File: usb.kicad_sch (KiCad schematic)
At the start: 16 parts, among them P1 USB_C_Plug_USB2.0, U1 MX6UL-VM, U4 TUSB320, U5 FPF2498BUCX, U6 TPD4EUSB30, U7 D5V0H1B2LP

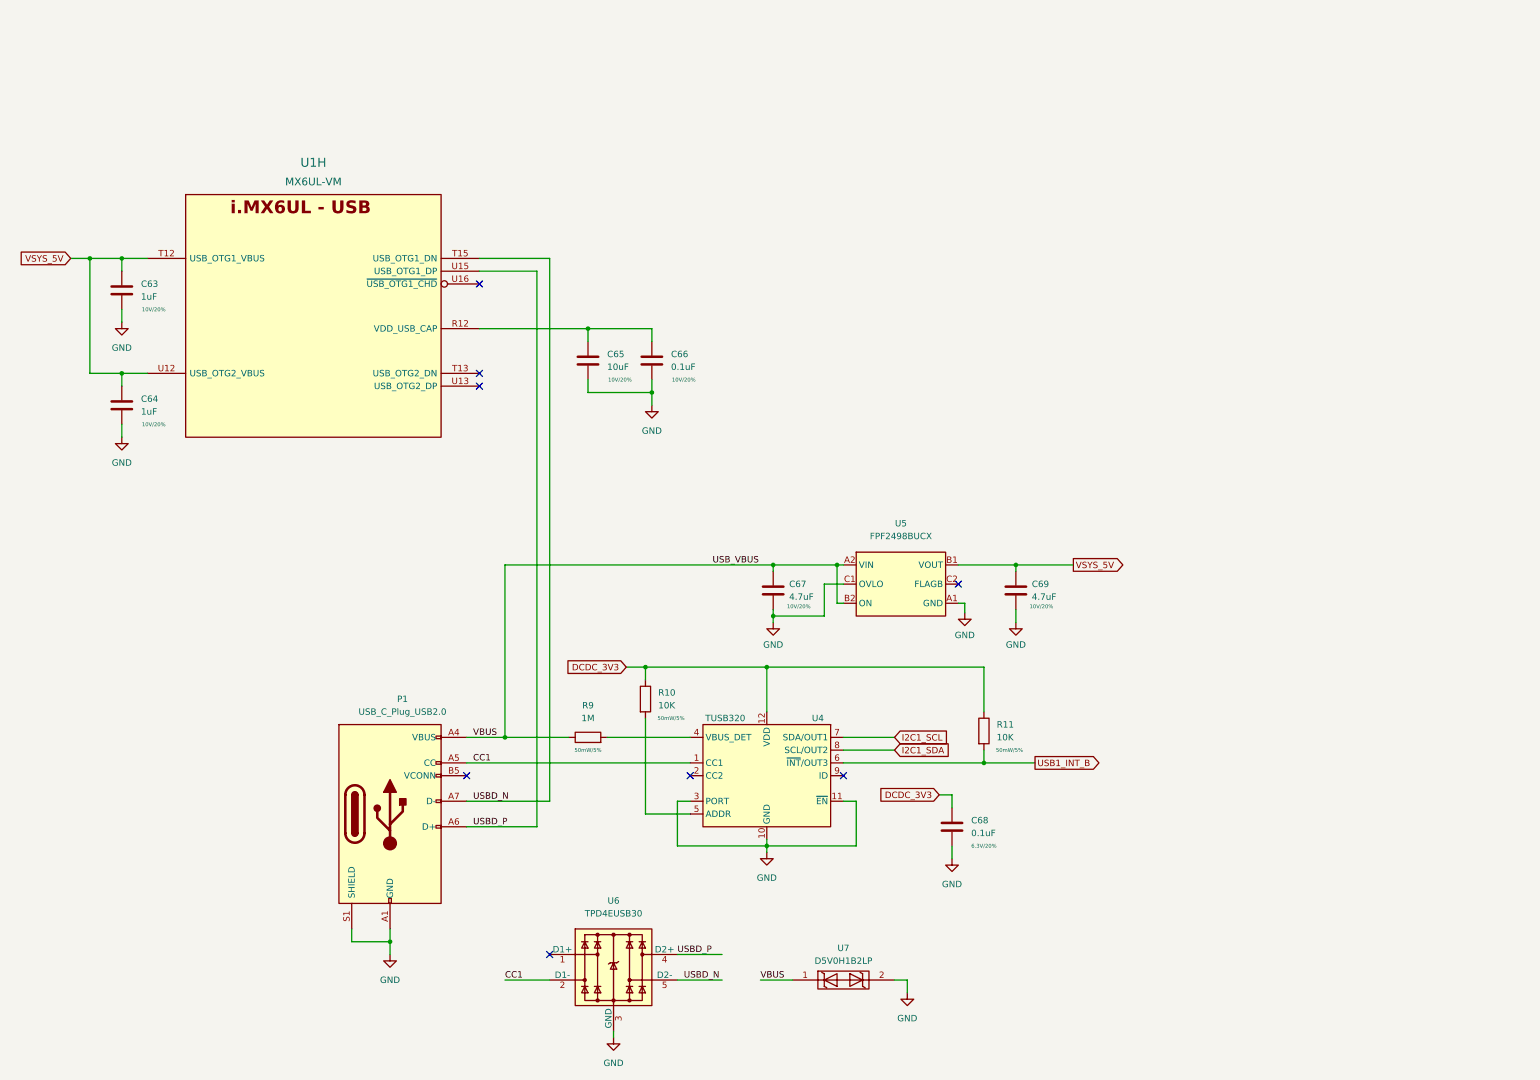
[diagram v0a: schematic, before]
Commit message: more ddr routing, add more connectors
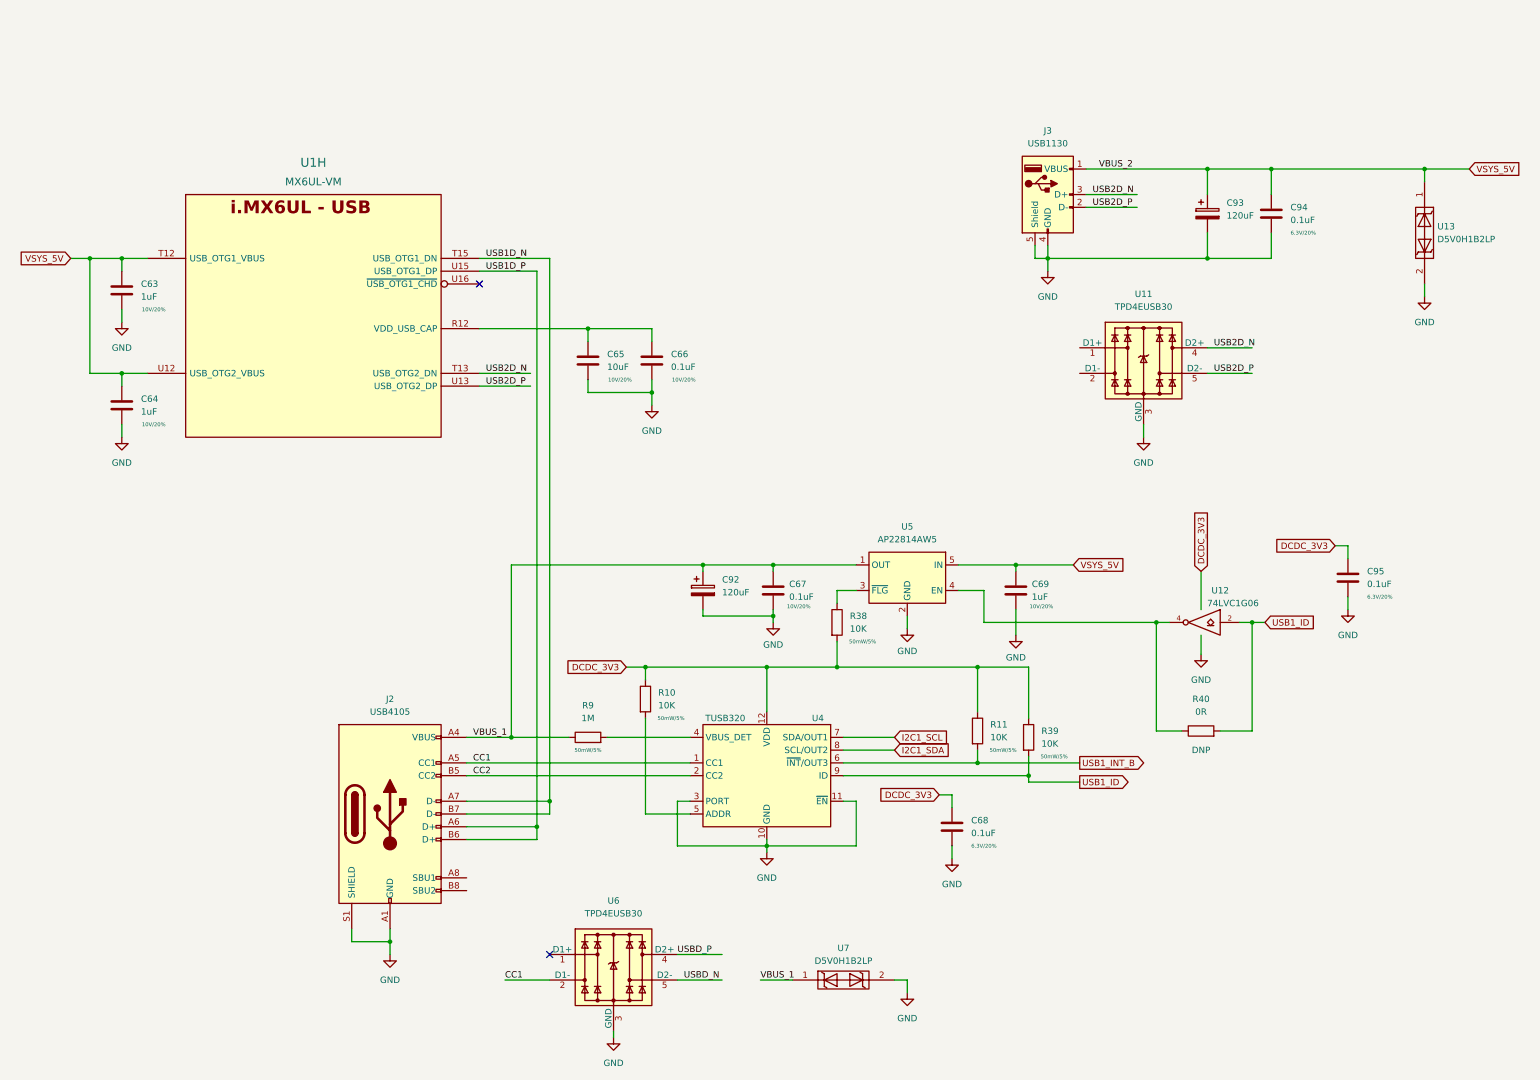
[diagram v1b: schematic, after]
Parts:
- removed P1: USB_C_Plug_USB2.0, Connector_USB:USB_C_Plug_Molex_105444, symbol Connector:USB_C_Plug_USB2.0
- removed U5: FPF2498BUCX, Package_CSP:WLCSP-6_1.4x1.0mm_P0.4mm, symbol imx6ull-sbc:FPF2498BUCX
- added C92, C93: 120uF, Capacitor_SMD:CP_Elec_5x5.8, symbol Device:C_Polarized
- added C94, C95: 0.1uF, Capacitor_SMD:C_0402_1005Metric, symbol Device:C
- added J2: USB4105, Connector_USB:USB_C_Receptacle_HRO_TYPE-C-31-M-12, symbol Connector:USB_C_Receptacle_USB2.0
- added J3: USB1130, imx6ull-sbc:GCT_USB1130-15-A_REVA, symbol Connector:USB_A
- added R38, R39: 10K, Resistor_SMD:R_0402_1005Metric, symbol Device:R
- added R40: 0R, Resistor_SMD:R_0402_1005Metric, symbol Device:R
- added U11: TPD4EUSB30, Package_SON:USON-10_2.5x1.0mm_P0.5mm, symbol imx6ull-sbc:TPD4EUSB30
- added U12: 74LVC1G06, Package_TO_SOT_SMD:SOT-23-5, symbol 74xGxx:74LVC1G06
- added U13: D5V0H1B2LP, imx6ull-sbc:DFN100X60X45-2N, symbol imx6ull-sbc:D5V0H1B2LP
- added U5: AP22814AW5, Package_TO_SOT_SMD:SOT-23-5, symbol Power_Management:AP22814AW5
- C66: footprint Capacitor_SMD:C_0402_1005Metric -> Capacitor_SMD:C_0201_0603Metric
- C67: value 4.7uF -> 0.1uF
- C69: value 4.7uF -> 1uF
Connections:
- net CC1: now also J2.A5 (CC1)
- net GND: now also C92.2, C93.2, C94.2, C95.2, J2.A1 (GND), J2.A12 (GND), J2.B1 (GND), J2.B12 (GND), J2.S1 (SHIELD), J3.4 (GND), J3.5 (Shield), U11.3 (GND), U11.8 (GND), U12.3 (GND), U13.2, U5.2 (GND)
- net USBD_N: no longer U1.T15 (USB_OTG1_DN)
- net USBD_P: no longer U1.U15 (USB_OTG1_DP)
- net VSYS_5V: now also C93.1, C94.1, J3.1 (VBUS), U13.1, U5.5 (IN)
- net USB2D_N: now reaches U1.T13 (USB_OTG2_DN)
- net USB2D_N: now also J3.3 (D+), U11.4 (D2+), U11.7
- net USB2D_P: now reaches U1.U13 (USB_OTG2_DP)
- net USB2D_P: now also J3.2 (D-), U11.5 (D2-), U11.6
- net CC2: now reaches U4.2 (CC2)
- net CC2: now also J2.B5 (CC2)
- net USB1_ID: now reaches U4.9 (ID)
- net USB1_ID: now also R39.2, R40.2, U12.2
- net DCDC_3V3 renamed VCC
- net VCC: now also C95.1, R38.2, R39.1, U12.5 (VCC)
- net USB_VBUS renamed VBUS_1
- net VBUS_1: now also C92.1, J2.A4 (VBUS), J2.A9 (VBUS), J2.B4 (VBUS), J2.B9 (VBUS), U5.1 (OUT)
- new net: R40.1, U12.4, U5.4 (EN)
- new net: R38.1, U5.3 (~{FLG})
- new net: U11.1 (D1+), U11.10
- new net: U11.2 (D1-), U11.9
- new net USB1D_N: J2.A7 (D-), J2.B7 (D-), U1.T15 (USB_OTG1_DN)
- new net USB1D_P: J2.A6 (D+), J2.B6 (D+), U1.U15 (USB_OTG1_DP)
- no-connect marks 8 -> 2
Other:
- moved on the sheet: R11

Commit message: start moving to hierarchal labels, add emmc
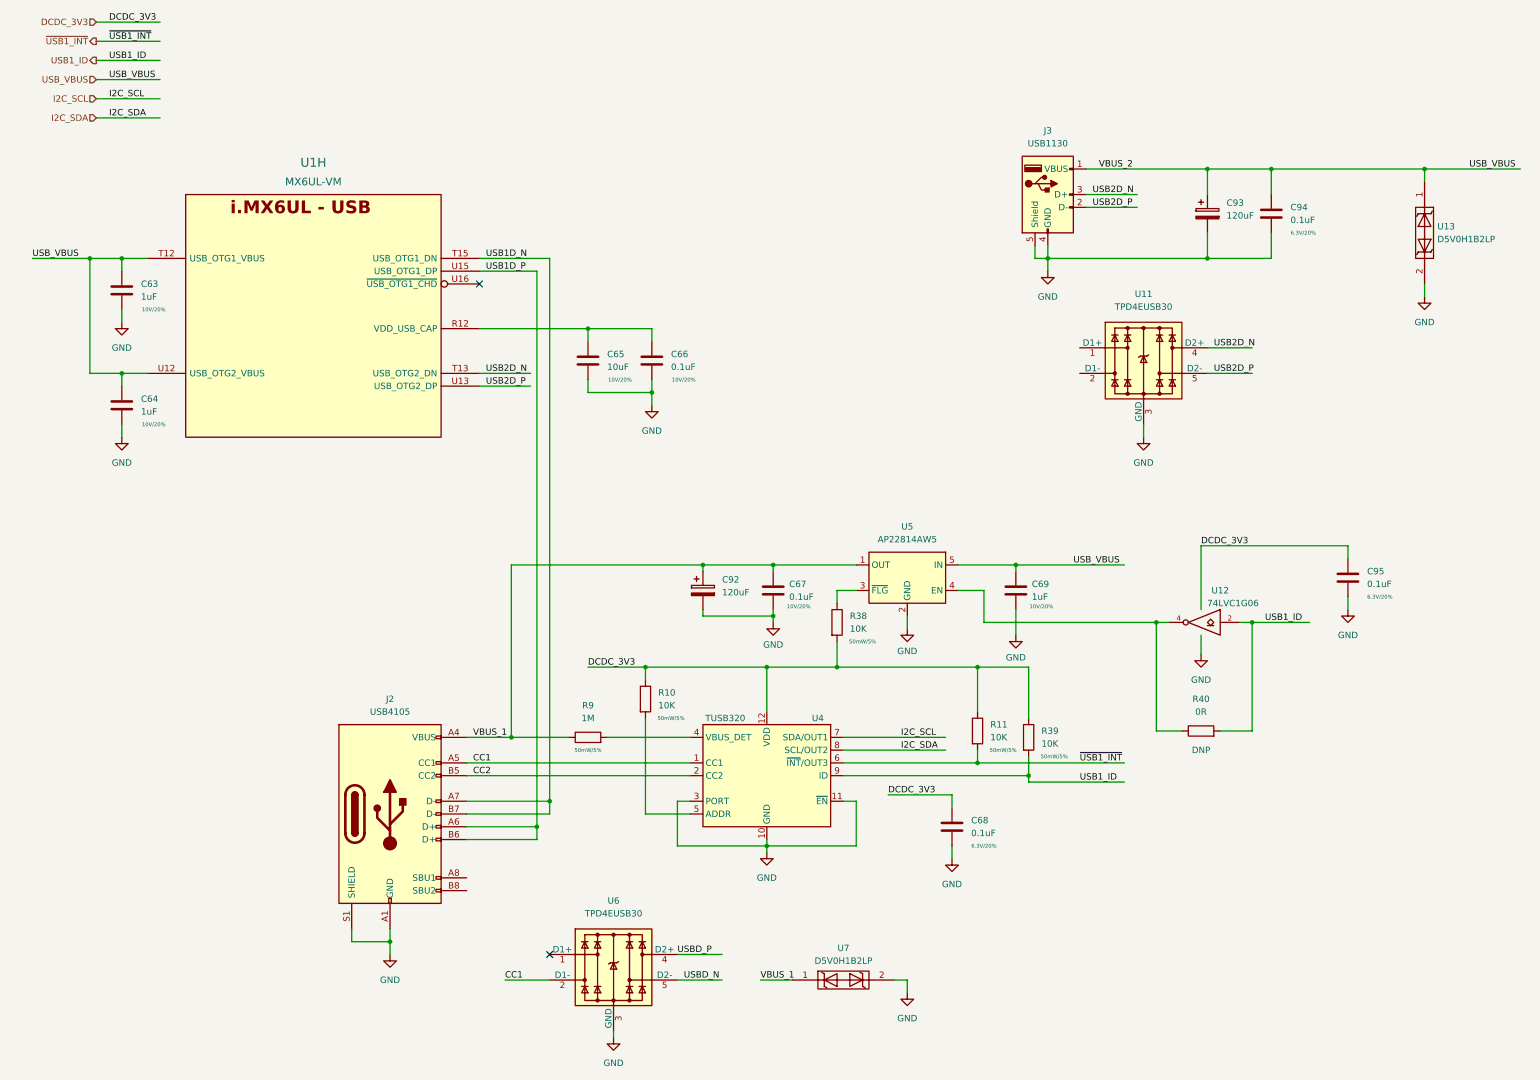
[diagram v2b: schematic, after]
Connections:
- net I2C1_SCL renamed I2C_SCL
- net I2C1_SDA renamed I2C_SDA
- net USB1_INT_B renamed ~{USB1_INT}
- net VSYS_5V renamed USB_VBUS
